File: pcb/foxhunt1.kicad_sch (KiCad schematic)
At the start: 0 parts

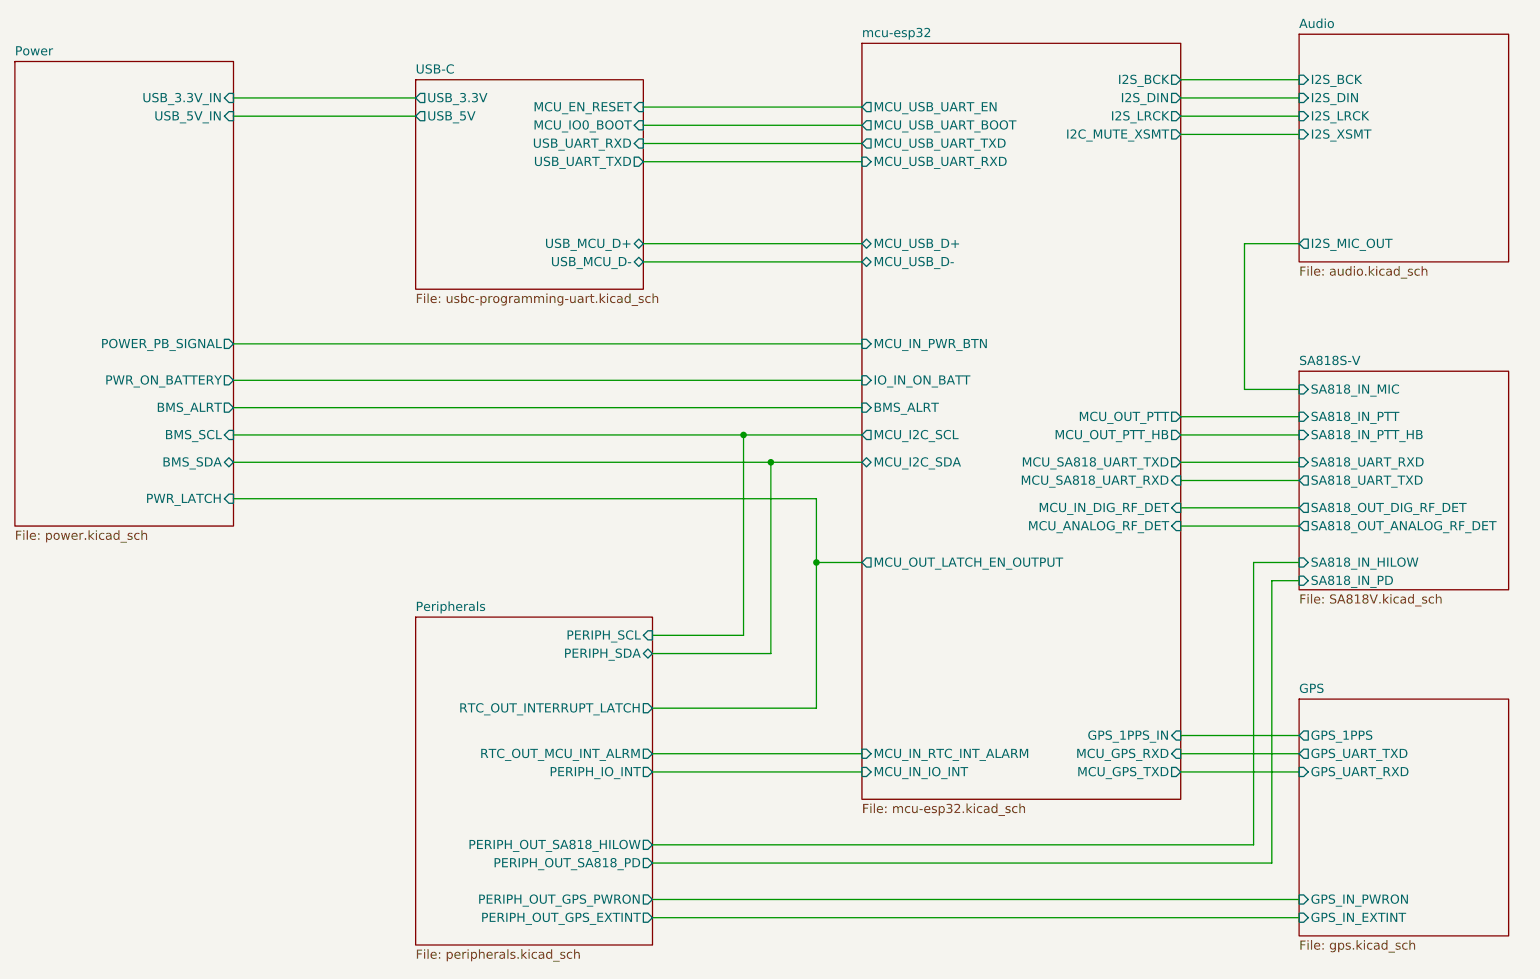
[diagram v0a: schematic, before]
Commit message: audio path
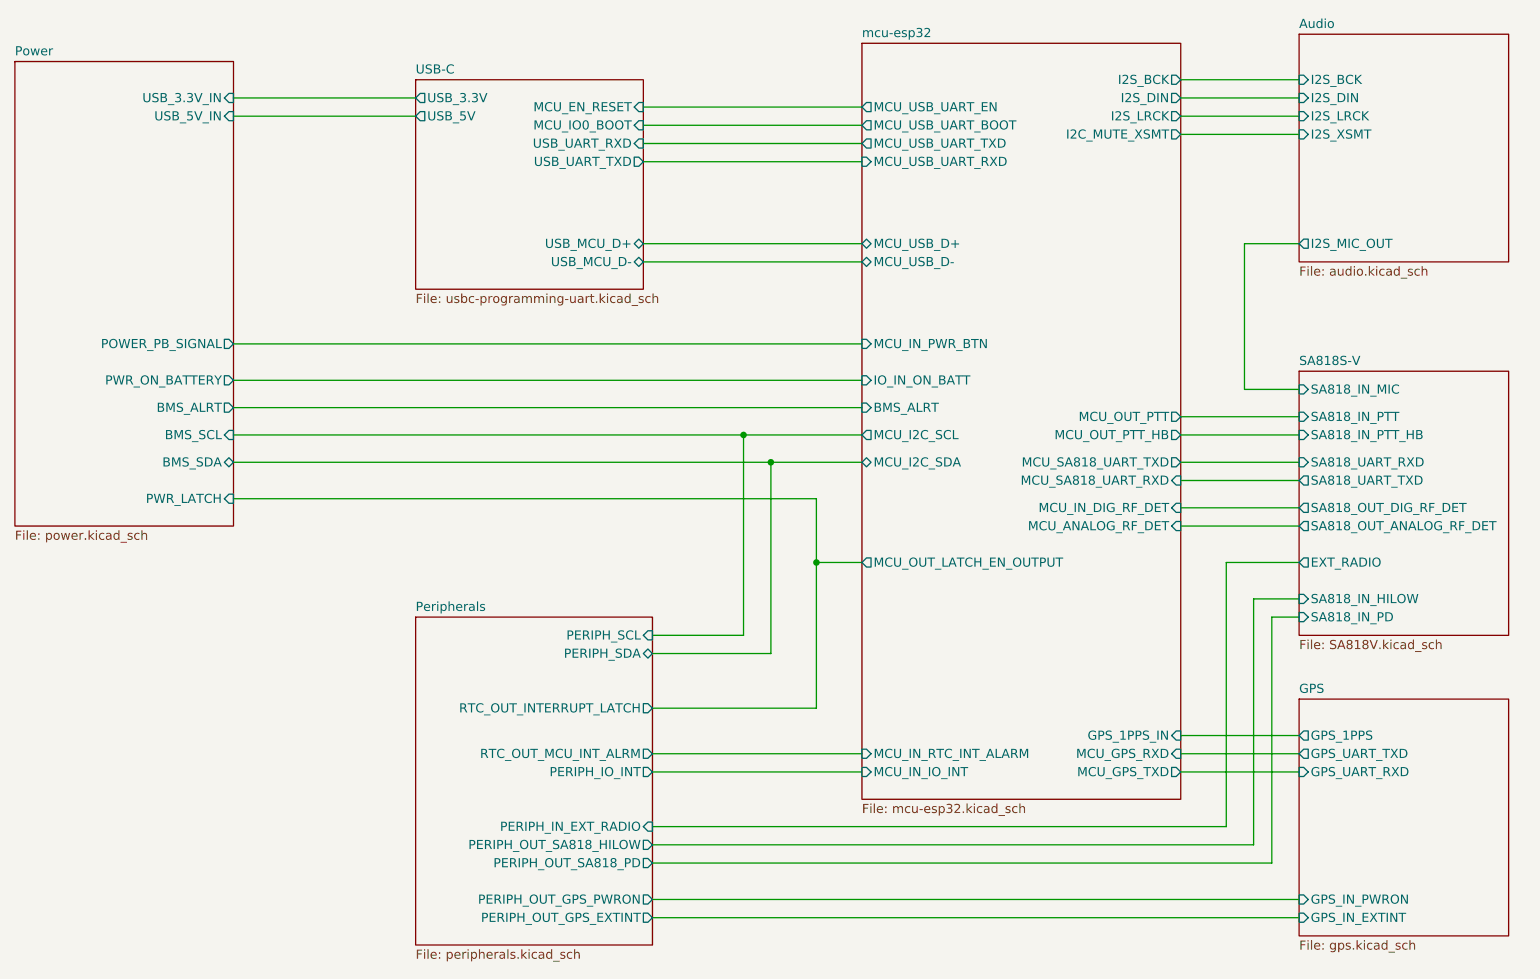
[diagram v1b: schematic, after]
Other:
- sheet Peripherals ports: added PERIPH_IN_EXT_RADIO; removed none
- sheet SA818S-V ports: added EXT_RADIO; removed none
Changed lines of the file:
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@@
 	(wire
 		(pts
-			(xy 220.98 105.41) (xy 220.98 144.78)
+			(xy 220.98 110.49) (xy 220.98 144.78)
 		)
 		(stroke
@@
 	(wire
 		(pts
-			(xy 227.33 105.41) (xy 220.98 105.41)
+			(xy 227.33 110.49) (xy 220.98 110.49)
 		)
 		(stroke
@@
 	(wire
 		(pts
+			(xy 217.17 105.41) (xy 217.17 142.24)
+		)
+		(stroke
+			(width 0)
+			(type default)
+		)
+	)
+	(wire
+		(pts
 			(xy 78.74 87.63) (xy 166.37 87.63)
 		)
@@
 	(wire
 		(pts
+			(xy 217.17 142.24) (xy 137.16 142.24)
+		)
+		(stroke
+			(width 0)
+			(type default)
+		)
+	)
+	(wire
+		(pts
 			(xy 210.82 45.72) (xy 227.33 45.72)
 		)
@@
 	(wire
 		(pts
-			(xy 223.52 147.32) (xy 223.52 107.95)
+			(xy 223.52 147.32) (xy 223.52 113.03)
 		)
 		(stroke
@@
 	(wire
 		(pts
-			(xy 223.52 107.95) (xy 227.33 107.95)
+			(xy 223.52 113.03) (xy 227.33 113.03)
+		)
+		(stroke
+			(width 0)
+			(type default)
+		)
+	)
+	(wire
+		(pts
+			(xy 227.33 105.41) (xy 217.17 105.41)
 		)
 		(stroke
@@
 	(sheet
 		(at 227.33 78.74)
-		(size 29.21 30.48)
+		(size 29.21 36.83)
 		(exclude_from_sim no)
 		(in_bom yes)
@@
 		)
 		(property "Sheetfile" "SA818V.kicad_sch"
-			(at 227.33 109.8046 0)
+			(at 227.33 116.1546 0)
 			(show_name no)
 			(do_not_autoplace no)
@@
 		)
 		(pin "SA818_IN_HILOW" input
-			(at 227.33 105.41 180)
+			(at 227.33 110.49 180)
 			(effects
 				(font
@@
 		)
 		(pin "SA818_IN_PD" input
-			(at 227.33 107.95 180)
+			(at 227.33 113.03 180)
 			(effects
 				(font
@@
 		(pin "SA818_IN_PTT" input
 			(at 227.33 85.09 180)
+			(effects
+				(font
+					(size 1.27 1.27)
+				)
+				(justify left)
+			)
+		)
+		(pin "EXT_RADIO" output
+			(at 227.33 105.41 180)
 			(effects
 				(font
@@
 			(effects
 				(font
+					(size 1.27 1.27)
+				)
+				(justify right)
+			)
+		)
+		(pin "PERIPH_IN_EXT_RADIO" input
+			(at 137.16 142.24 0)
+			(effects
+				(font

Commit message: annotations
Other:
- sheet Peripherals ports: added none; removed PERIPH_IN_EXT_RADIO, PERIPH_OUT_GPS_EXTINT
- sheet SA818S-V ports: added none; removed SA818_OUT_ANALOG_RF_DET, SA818_OUT_DIG_RF_DET
- sheet mcu-esp32 ports: added MCU_IN_EXT_RADIO, MCU_OUT_GPS_EXTINT; removed MCU_ANALOG_RF_DET, MCU_IN_DIG_RF_DET
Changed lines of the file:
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@@
 	)
 	(junction
-		(at 160.02 105.41)
+		(at 160.02 109.22)
 		(diameter 0)
 		(color 0 0 0 0)
@@
 	(wire
 		(pts
+			(xy 160.02 96.52) (xy 160.02 125.73)
+		)
+		(stroke
+			(width 0)
+			(type default)
+		)
+	)
+	(wire
+		(pts
 			(xy 135.89 60.96) (xy 166.37 60.96)
 		)
@@
 	(wire
 		(pts
-			(xy 210.82 97.79) (xy 227.33 97.79)
-		)
-		(stroke
-			(width 0)
-			(type default)
-		)
-	)
-	(wire
-		(pts
 			(xy 137.16 152.4) (xy 227.33 152.4)
 		)
@@
 	(wire
 		(pts
-			(xy 217.17 105.41) (xy 217.17 142.24)
-		)
-		(stroke
-			(width 0)
-			(type default)
-		)
-	)
-	(wire
-		(pts
 			(xy 78.74 87.63) (xy 166.37 87.63)
 		)
@@
 	(wire
 		(pts
-			(xy 160.02 96.52) (xy 160.02 105.41)
-		)
-		(stroke
-			(width 0)
-			(type default)
-		)
-	)
-	(wire
-		(pts
-			(xy 137.16 154.94) (xy 227.33 154.94)
-		)
-		(stroke
-			(width 0)
-			(type default)
-		)
-	)
-	(wire
-		(pts
 			(xy 210.82 87.63) (xy 227.33 87.63)
 		)
@@
 	(wire
 		(pts
-			(xy 160.02 105.41) (xy 166.37 105.41)
+			(xy 160.02 109.22) (xy 166.37 109.22)
 		)
 		(stroke
@@
 	(wire
 		(pts
-			(xy 217.17 142.24) (xy 137.16 142.24)
-		)
-		(stroke
-			(width 0)
-			(type default)
-		)
-	)
-	(wire
-		(pts
 			(xy 210.82 45.72) (xy 227.33 45.72)
 		)
@@
 	(wire
 		(pts
-			(xy 160.02 105.41) (xy 160.02 125.73)
+			(xy 210.82 127) (xy 227.33 127)
 		)
 		(stroke
@@
 	(wire
 		(pts
+			(xy 210.82 105.41) (xy 227.33 105.41)
+		)
+		(stroke
+			(width 0)
+			(type default)
+		)
+	)
+	(wire
+		(pts
 			(xy 78.74 83.82) (xy 166.37 83.82)
 		)
@@
 		(pts
 			(xy 223.52 113.03) (xy 227.33 113.03)
-		)
-		(stroke
-			(width 0)
-			(type default)
-		)
-	)
-	(wire
-		(pts
-			(xy 227.33 105.41) (xy 217.17 105.41)
-		)
-		(stroke
-			(width 0)
-			(type default)
-		)
-	)
-	(wire
-		(pts
-			(xy 210.82 100.33) (xy 227.33 100.33)
 		)
 		(stroke
@@
 		)
 		(pin "GPS_IN_EXTINT" input
-			(at 227.33 154.94 180)
+			(at 227.33 127 180)
 			(effects
 				(font
@@
 			)
 		)
-		(pin "SA818_OUT_ANALOG_RF_DET" output
-			(at 227.33 100.33 180)
-			(effects
-				(font
-					(size 1.27 1.27)
-				)
-				(justify left)
-			)
-		)
-		(pin "SA818_OUT_DIG_RF_DET" output
-			(at 227.33 97.79 180)
-			(effects
-				(font
-					(size 1.27 1.27)
-				)
-				(justify left)
-			)
-		)
 		(pin "SA818_IN_PTT_HB" input
 			(at 227.33 87.63 180)
@@
 		)
 		(pin "MCU_OUT_LATCH_EN_OUTPUT" output
-			(at 166.37 105.41 180)
+			(at 166.37 109.22 180)
 			(effects
 				(font
@@
 			)
 		)
-		(pin "MCU_ANALOG_RF_DET" input
-			(at 210.82 100.33 0)
-			(effects
-				(font
-					(size 1.27 1.27)
-				)
-				(justify right)
-			)
-		)
-		(pin "MCU_IN_DIG_RF_DET" input
-			(at 210.82 97.79 0)
-			(effects
-				(font
-					(size 1.27 1.27)
-				)
-				(justify right)
-			)
-		)
 		(pin "MCU_OUT_PTT_HB" output
 			(at 210.82 87.63 0)
+			(effects
+				(font
+					(size 1.27 1.27)
+				)
+				(justify right)
+			)
+		)
+		(pin "MCU_IN_EXT_RADIO" input
+			(at 210.82 105.41 0)
+			(effects
+				(font
+					(size 1.27 1.27)
+				)
+				(justify right)
+			)
+		)
+		(pin "MCU_OUT_GPS_EXTINT" output
+			(at 210.82 127 0)
 			(effects
 				(font
@@
 			(effects
 				(font
-					(size 1.27 1.27)
-				)
-				(justify right)
-			)
-		)
-		(pin "PERIPH_OUT_GPS_EXTINT" output
-			(at 137.16 154.94 0)
-			(effects
-				(font
-					(size 1.27 1.27)
-				)
-				(justify right)
-			)
-		)
-		(pin "PERIPH_IN_EXT_RADIO" input
-			(at 137.16 142.24 0)
-			(effects
-				(font

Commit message: changes on pcb
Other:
- sheet Power ports: added USB_5V_SW; removed USB_5V_IN
- sheet USB-C ports: added USB_5V_SW; removed USB_5V
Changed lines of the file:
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@@
-			)
-		)
-		(pin "USB_5V_IN" input
-			(at 78.74 43.18 0)
-			(effects
-				(font
-					(size 1.27 1.27)
-				)
-				(justify right)
 			)
 		)
@@
 		(pin "POWER_PB_SIGNAL" output
 			(at 78.74 74.93 0)
+			(effects
+				(font
+					(size 1.27 1.27)
+				)
+				(justify right)
+			)
+		)
+		(pin "USB_5V_SW" input
+			(at 78.74 43.18 0)
 			(effects
 				(font
@@
 			)
 		)
-		(pin "USB_5V" output
-			(at 104.14 43.18 180)
-			(effects
-				(font
-					(size 1.27 1.27)
-				)
-				(justify left)
-			)
-		)
 		(pin "USB_MCU_D+" bidirectional
 			(at 135.89 60.96 0)
@@
 			)
 		)
+		(pin "USB_5V_SW" output
+			(at 104.14 43.18 180)
+			(effects
+				(font
+					(size 1.27 1.27)
+				)
+				(justify left)
+			)
+		)
